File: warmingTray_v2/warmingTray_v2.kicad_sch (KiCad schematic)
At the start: 22 parts, among them J1 Jack-DC, P1 Power, P2 Analog, P3 Analog, P4 Digital, P5 PWM, P6 PWM, P7 Communication

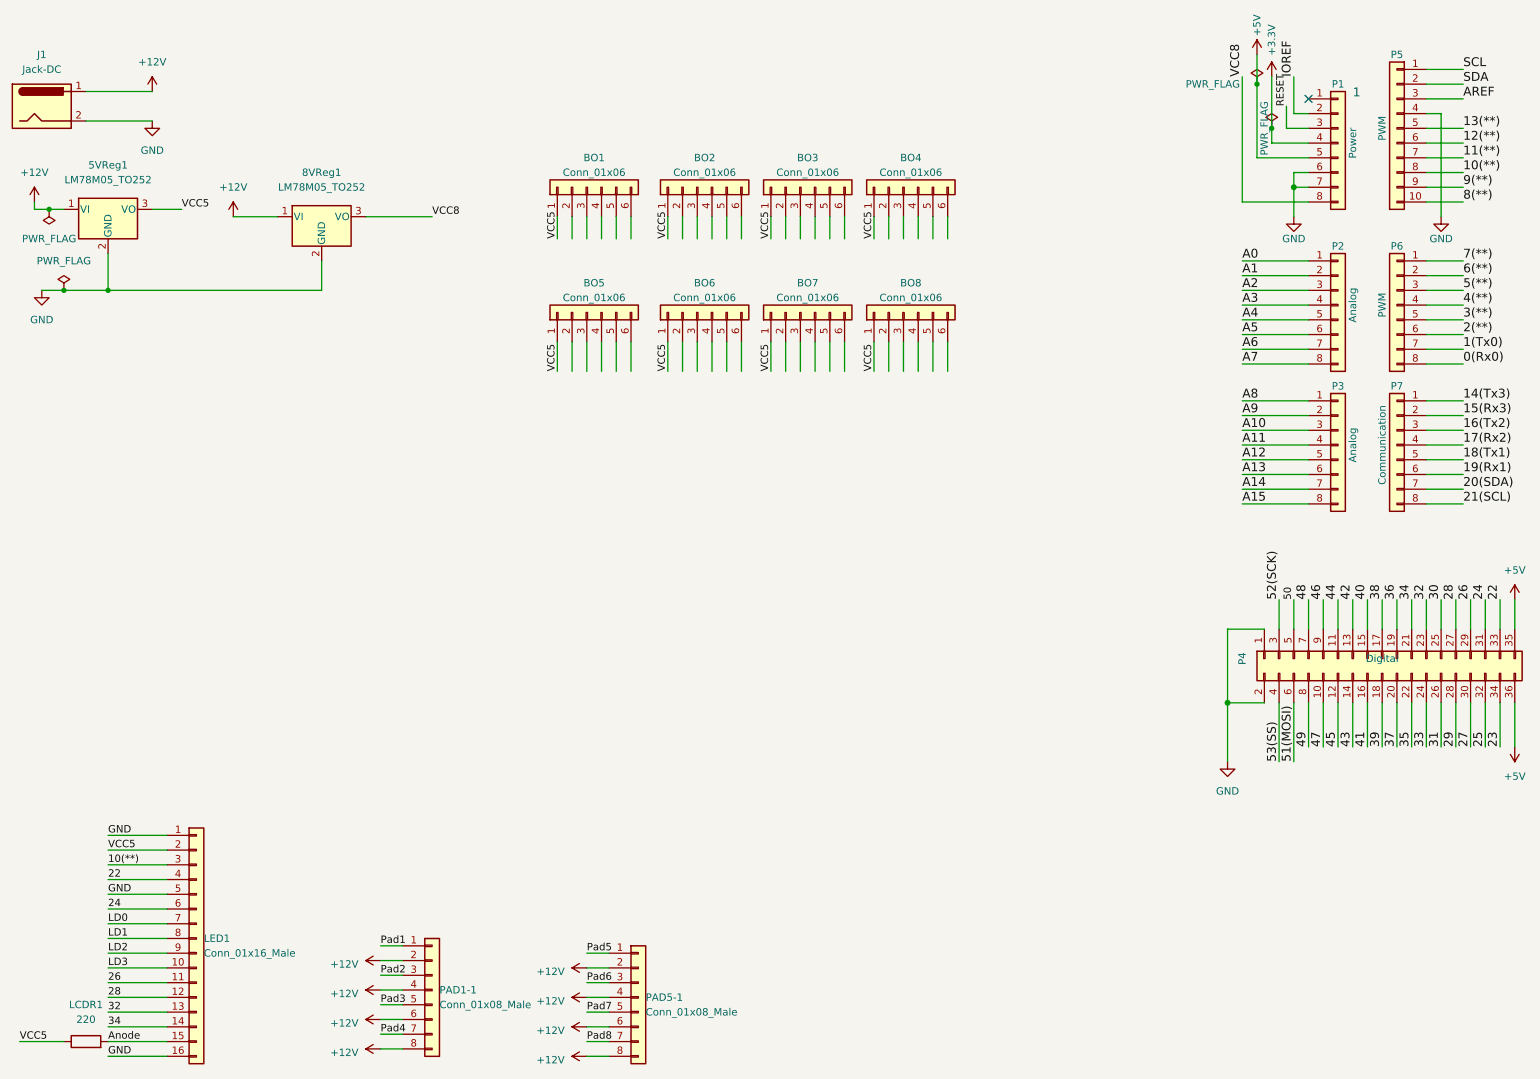
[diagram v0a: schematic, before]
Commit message: PCB Update: added transistors and pinouts
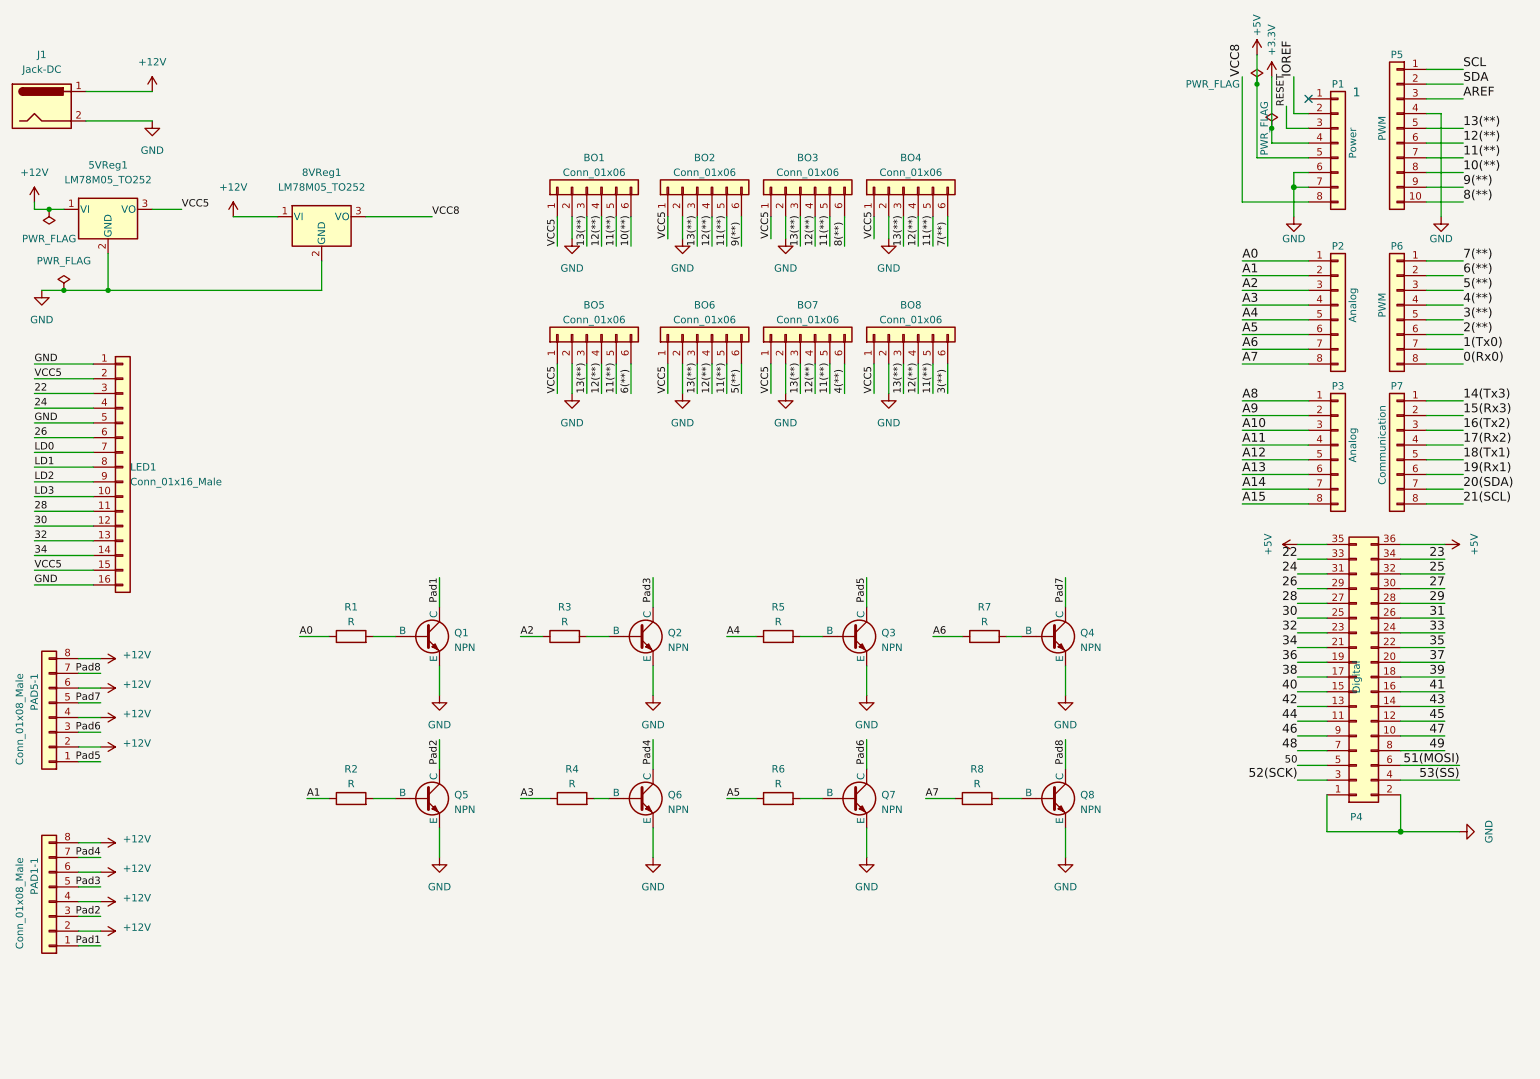
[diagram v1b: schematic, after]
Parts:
- removed LCDR1: 220, Resistor_SMD:R_0805_2012Metric, symbol Device:R
- added Q1, Q2, Q3, Q4, Q5, Q6, Q7, Q8: NPN, symbol Simulation_SPICE:NPN
- added R1, R2, R3, R4, R5, R6, R7, R8: R, symbol Device:R
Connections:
- net Anode is gone; now on net VCC5: LED1.15 (Pin_15)
- net 10(**): now also BO1.6 (Pin_6); no longer LED1.3 (Pin_3)
- net 11(**): now also BO1.5 (Pin_5), BO2.5 (Pin_5), BO3.5 (Pin_5), BO4.5 (Pin_5), BO5.5 (Pin_5), BO6.5 (Pin_5), BO7.5 (Pin_5), BO8.5 (Pin_5)
- net 12(**): now also BO1.4 (Pin_4), BO2.4 (Pin_4), BO3.4 (Pin_4), BO4.4 (Pin_4), BO5.4 (Pin_4), BO6.4 (Pin_4), BO7.4 (Pin_4), BO8.4 (Pin_4)
- net 13(**): now also BO1.3 (Pin_3), BO2.3 (Pin_3), BO3.3 (Pin_3), BO4.3 (Pin_3), BO5.3 (Pin_3), BO6.3 (Pin_3), BO7.3 (Pin_3), BO8.3 (Pin_3)
- net 22: now also LED1.3 (Pin_3); no longer LED1.4 (Pin_4)
- net 24: now also LED1.4 (Pin_4); no longer LED1.6 (Pin_6)
- net 26: now also LED1.6 (Pin_6); no longer LED1.11 (Pin_11)
- net 28: now also LED1.11 (Pin_11); no longer LED1.12 (Pin_12)
- net 3(**): now also BO8.6 (Pin_6)
- net 30: now also LED1.12 (Pin_12)
- net 4(**): now also BO7.6 (Pin_6)
- net 5(**): now also BO6.6 (Pin_6)
- net 6(**): now also BO5.6 (Pin_6)
- net 7(**): now also BO4.6 (Pin_6)
- net 8(**): now also BO3.6 (Pin_6)
- net 9(**): now also BO2.6 (Pin_6)
- net A0: now also R1.1
- net A1: now also R2.1
- net A2: now also R3.1
- net A3: now also R4.1
- net A4: now also R5.1
- net A5: now also R6.1
- net A6: now also R7.1
- net A7: now also R8.1
- net GND: now also BO1.2 (Pin_2), BO2.2 (Pin_2), BO3.2 (Pin_2), BO4.2 (Pin_2), BO5.2 (Pin_2), BO6.2 (Pin_2), BO7.2 (Pin_2), BO8.2 (Pin_2), Q1.3 (E), Q2.3 (E), Q3.3 (E), Q4.3 (E), Q5.3 (E), Q6.3 (E), Q7.3 (E), Q8.3 (E)
- net Pad1: now also Q1.1 (C)
- net Pad2: now also Q5.1 (C)
- net Pad3: now also Q2.1 (C)
- net Pad4: now also Q6.1 (C)
- net Pad5: now also Q3.1 (C)
- net Pad6: now also Q7.1 (C)
- net Pad7: now also Q4.1 (C)
- net Pad8: now also Q8.1 (C)
- new net: Q4.2 (B), R7.2
- new net: Q5.2 (B), R2.2
- new net: Q6.2 (B), R4.2
- new net: Q1.2 (B), R1.2
- new net: Q8.2 (B), R8.2
- new net: Q2.2 (B), R3.2
- new net: Q7.2 (B), R6.2
- new net: Q3.2 (B), R5.2
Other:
- moved on the sheet: BO5, BO6, BO7, BO8, LED1, P4, PAD1-1, PAD5-1
